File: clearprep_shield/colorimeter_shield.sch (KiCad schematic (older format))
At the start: 7 parts, among them K1 CONN_3, P1 CONN_4, P2 CONN_5X2, P4 CONN_2

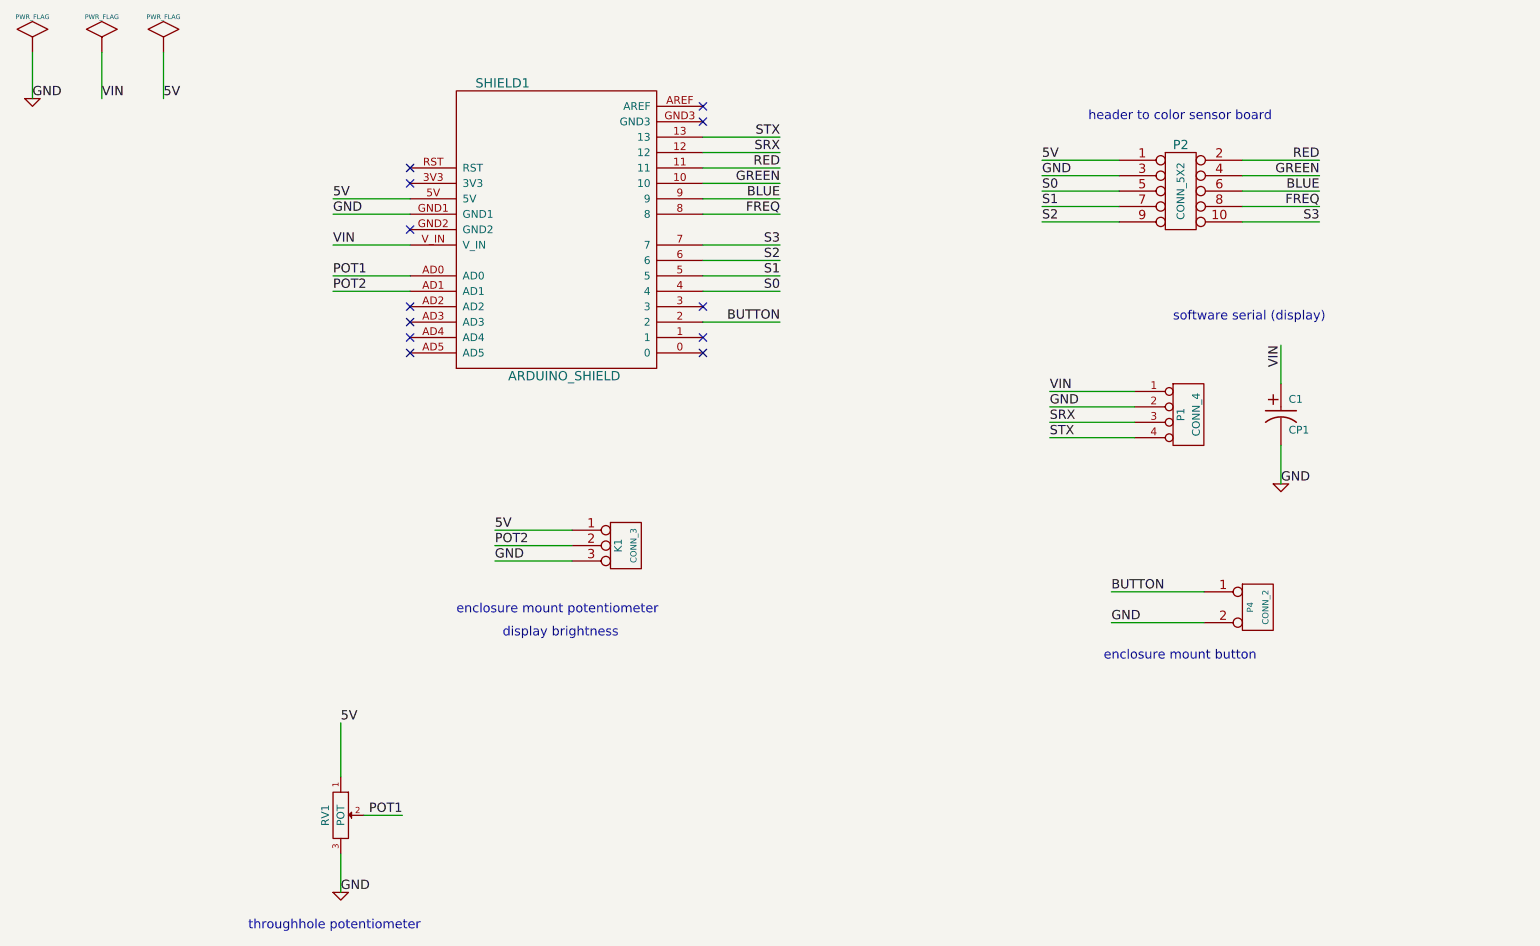
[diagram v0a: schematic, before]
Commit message: Designed ardiuno sheild for clearprep device.
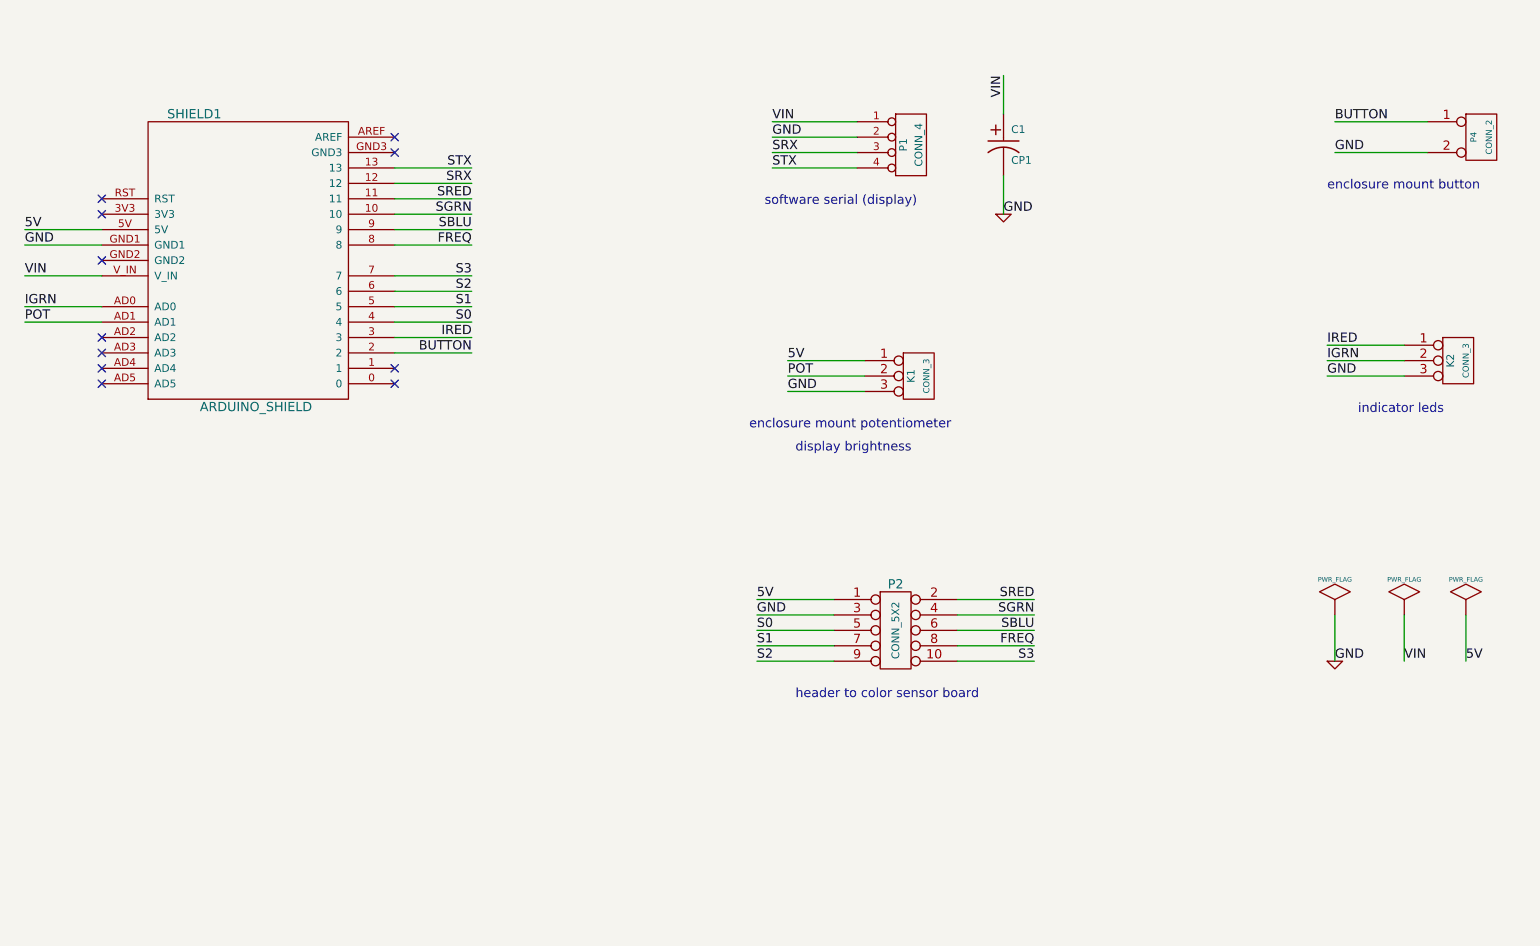
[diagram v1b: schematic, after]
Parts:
- removed RV1: POT, symbol POT
- added K2: CONN_3, symbol CONN_3
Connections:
- net GND: now also K2.3 (P3)
- net IRED: now reaches SHIELD1.3
- net IRED: now also K2.1 (P1)
- net BLUE renamed SBLU
- net GREEN renamed SGRN
- net POT1 renamed IGRN
- net IGRN: now also K2.2 (PM)
- net POT2 renamed POT
- net RED renamed SRED
- no-connect marks 12 -> 11
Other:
- note added: "indicator leds"
- note removed: "throughhole potentiometer"
- moved on the sheet: C1, K1, P1, P2, P4, SHIELD1

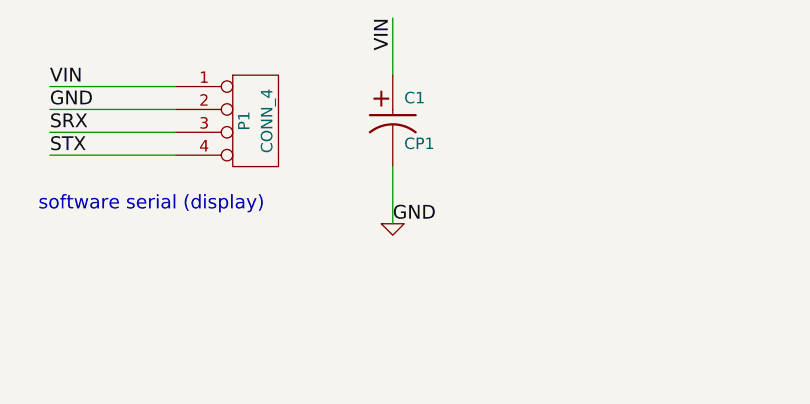
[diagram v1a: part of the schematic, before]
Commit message: Modified firmware so that threshold is displayed in measurement mode and so that there are only two modes: measurement and set threhold.
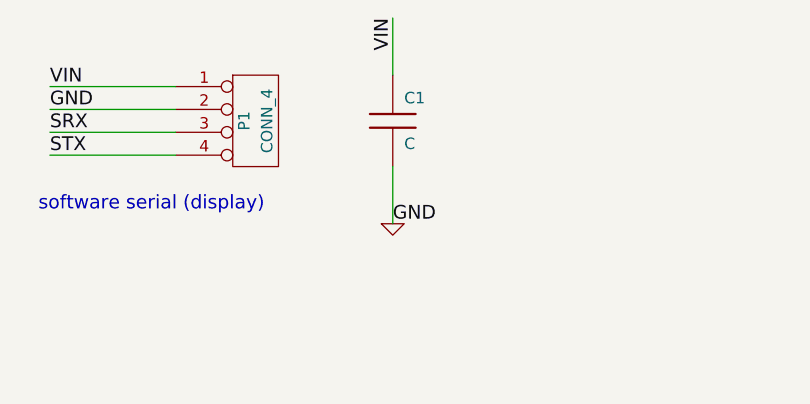
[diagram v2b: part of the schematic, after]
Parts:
- removed C1: CP1, symbol CP1
- added C1: C, symbol C
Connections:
- net GND: now also C1.2
- net VIN: now also C1.1
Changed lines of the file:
@@
-	1    0    0    -1
-$EndComp
-$Comp
-L CP1 C1
-U 1 1 4F04AA4F
-P 7000 1350
-F 0 "C1" H 7050 1450 50  0000 L CNN
-F 1 "CP1" H 7050 1250 50  0000 L CNN
-F 2 "" H 7000 1350 60  0001 C CNN
-F 3 "" H 7000 1350 60  0001 C CNN
-	1    7000 1350
 	1    0    0    -1
 $EndComp
@@
 Text Label 9100 2650 0    60   ~ 0
 IRED
+$Comp
+L C C1
+U 1 1 51B8E8C5
+P 7000 1350
+F 0 "C1" H 7050 1450 50  0000 L CNN
+F 1 "C" H 7050 1250 50  0000 L CNN
+F 2 "" H 7000 1350 60  0000 C CNN
+F 3 "" H 7000 1350 60  0000 C CNN
+	1    7000 1350
+	1    0    0    -1
+$EndComp
 $EndSCHEMATC
